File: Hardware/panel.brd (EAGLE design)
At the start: 79 x 43 mm, 86 parts, among them Q1 BC817-40LT1SMD, Q10 BC807-16LT1SMD, Q11 BC807-16LT1SMD, Q12 BC807-16LT1SMD, Q13 BC817-40LT1SMD, Q14 BC817-40LT1SMD, Q15 BC817-40LT1SMD, Q16 BC817-40LT1SMD, Q17 BC817-40LT1SMD, Q18 BC817-40LT1SMD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

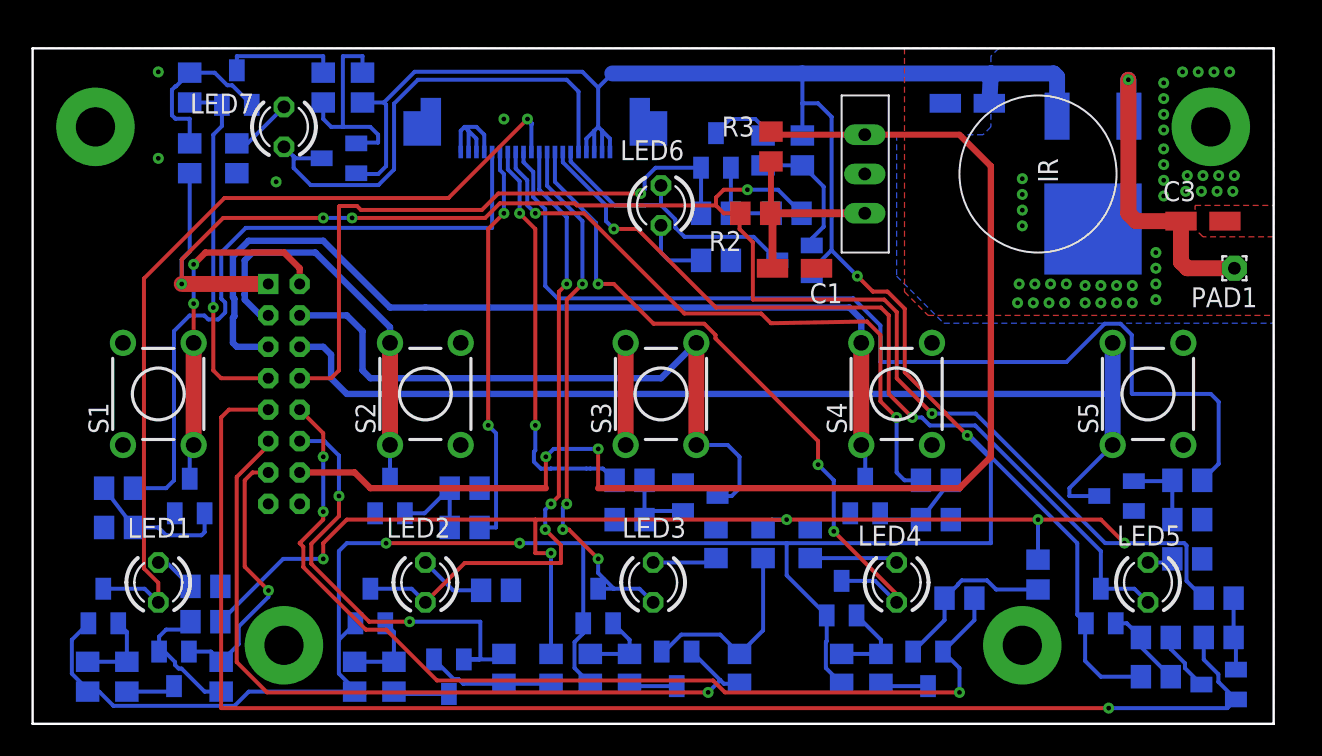
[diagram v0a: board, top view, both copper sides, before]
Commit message: по результатам эксперимента с кнопками и индикаторами все нормально. оявилась идея добавить защитные резисторы на индикаторные выходы,чтобы не сгорал транзистор в случае кз на землю
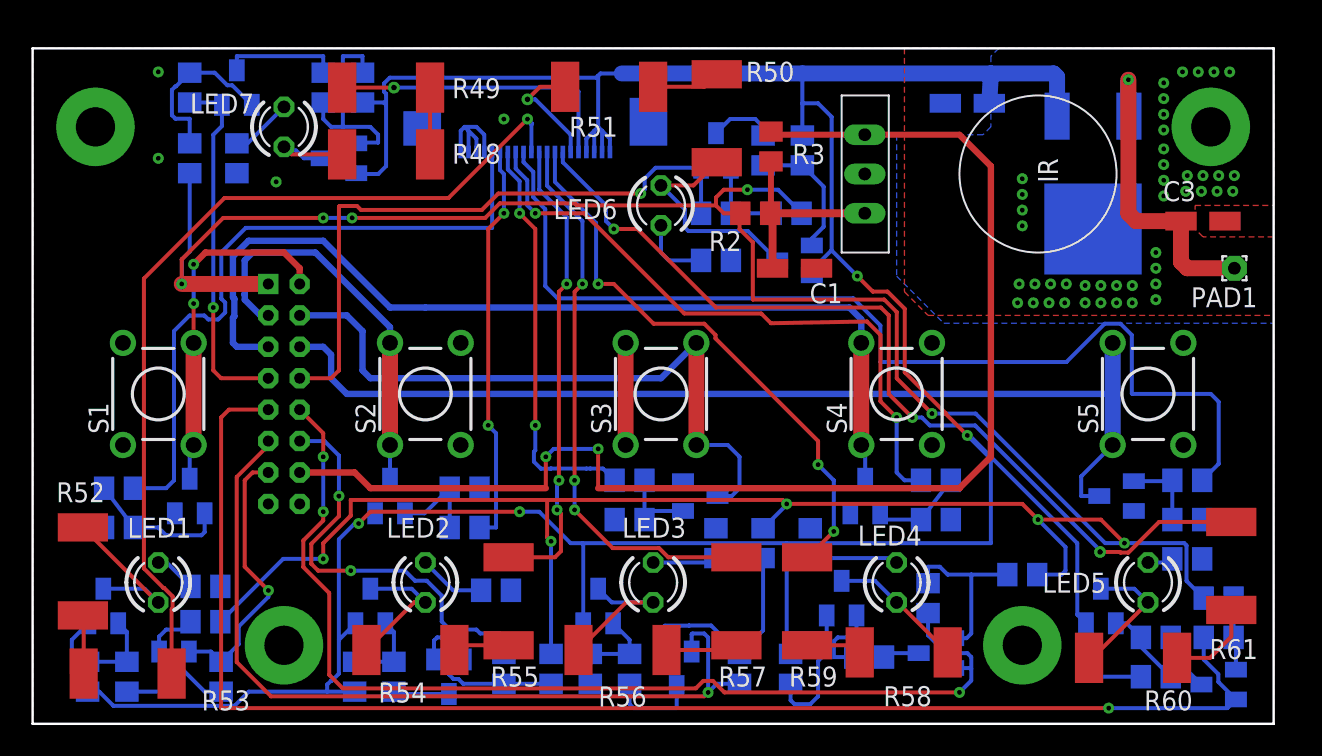
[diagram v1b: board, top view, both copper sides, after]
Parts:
- added R48, R49, R50, R51, R52, R53, R54, R55, R56, R57, R58, R59, R60, R61: 150, rcl:R2512
- moved R30 3.25 mm to (47.2, 2.50), turned to 90 degrees
- moved R40 2.00 mm to (56.0, 7.00), turned to 270 degrees
- moved Q16 1.12 mm to (56.5, 3.50), turned to 270 degrees
- moved R28 1.06 mm to (52.2, 3.25), turned to 180 degrees
- moved R41 1.00 mm to (62.0, 8.50), turned to 0 degrees
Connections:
- new net N$3: LED7.A, Q6.3, R48.1
- new net N$36: R48.2, R49.1
- new net N$37: LED6.A, Q7.3, R50.1
- new net N$38: R50.2, R51.1
- new net N$39: LED1.A, Q8.3, R52.1
- new net N$40: R52.2, R53.1
- new net N$41: LED2.A, Q9.3, R54.1
- new net N$42: R54.2, R55.1
- new net N$43: LED3.A, Q10.3, R56.1
- new net N$44: R56.2, R57.1
- new net N$45: LED4.A, Q11.3, R58.1
- new net N$46: R58.2, R59.1
- new net N$47: LED5.A, Q12.3, R60.1
- new net N$48: R60.2, R61.1
- net ADJLED_SIG: now also R55.2; no longer LED2.A, Q9.3
- net DOWNLED_SIG: now also R57.2; no longer LED3.A, Q10.3
- net LVLLED_SIG: now also R49.2; no longer LED7.A, Q6.3
- net PWRLED_SIG: now also R53.2; no longer LED1.A, Q8.3
- net UPLED_SIG: now also R51.2; no longer LED6.A, Q7.3
- net XLED_SIG: now also R59.2; no longer LED4.A, Q11.3
- net YLED_SIG: now also R61.2; no longer LED5.A, Q12.3
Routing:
- net N$37: track 0.00 -> 14.2 mm
- net LVLLED_SIG: track 31.4 -> 19.0 mm, vias 0 -> 1
- net ADJLED_SIG: track 41.4 -> 30.0 mm
- net N$39: track 0.00 -> 10.6 mm
- net UPLED_SIG: track 17.9 -> 7.51 mm, vias 0 -> 1
- net N$43: track 0.00 -> 9.87 mm
- net N$41: track 0.00 -> 8.87 mm
- net N$45: track 0.00 -> 8.63 mm
- net N$47: track 0.00 -> 8.57 mm
- net XLED_SIG: track 44.2 -> 36.4 mm
- net N$3: track 0.00 -> 6.60 mm
- net N$20: track 5.59 -> 11.5 mm
- net +5V: track 179.9 -> 185.7 mm
- net N$48: track 0.00 -> 5.71 mm
- net XLED: track 63.7 -> 68.3 mm
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
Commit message: подготовил файлы для заказа в электроконнекте,а так же сделал пдф со списком компонентов
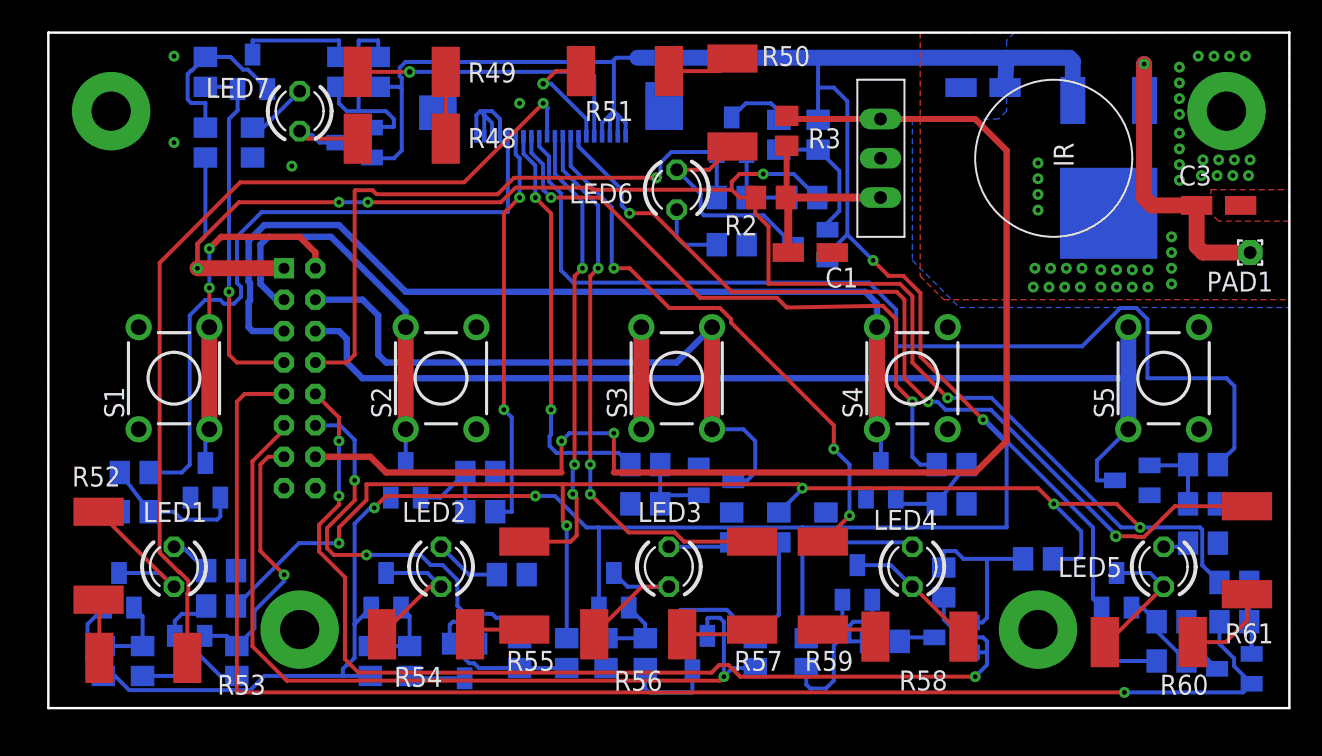
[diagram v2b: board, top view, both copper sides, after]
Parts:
- moved C1 1.41 mm to (48.5, 29.0)
- moved C2 1.41 mm to (59.5, 39.5)
- moved C3 1.41 mm to (74.5, 32.0)
- moved LED1 1.41 mm to (8.00, 9.00)
- moved LED2 1.41 mm to (25.0, 9.00)
- moved LED3 1.41 mm to (39.5, 9.00)
- moved LED4 1.41 mm to (55.0, 9.00)
- moved LED5 1.41 mm to (71.0, 9.00)
- moved LED6 1.41 mm to (40.0, 33.0)
- moved LED7 1.41 mm to (16.0, 38.0)
- moved PAD1 1.41 mm to (76.5, 29.0)
- moved Q1 1.41 mm to (10.0, 14.5)
- moved Q10 1.41 mm to (36.0, 7.50)
- moved Q11 1.41 mm to (51.5, 8.00)
- moved Q12 1.41 mm to (68.0, 7.50)
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
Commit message: по требованию с производства увеличил зазорполигона до 0,2мм на обеих платах. заказ переделал. заказе указал покрытие ПОС 63 вместо имерсионного олова
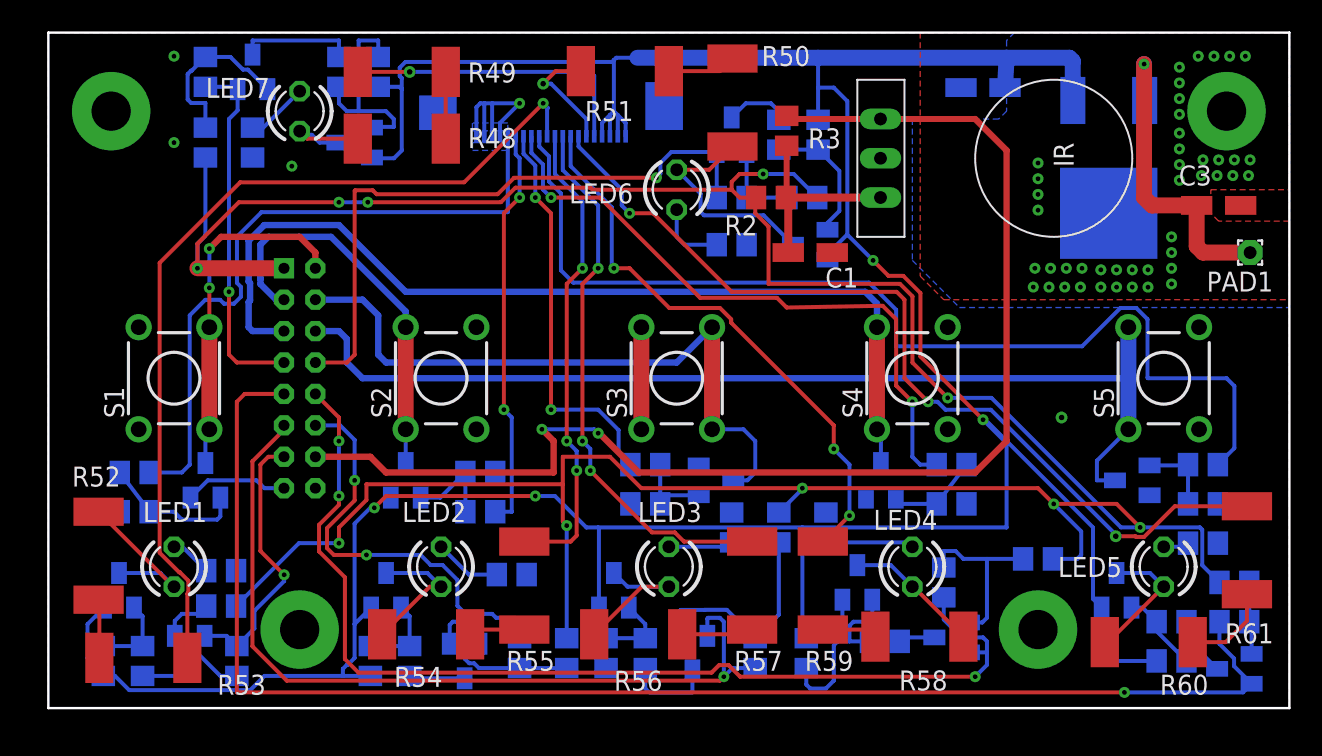
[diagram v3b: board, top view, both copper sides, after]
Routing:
- net GND: track 14.0 -> 24.6 mm, vias 52 -> 53
- net +5V: track 185.7 -> 188.1 mm
- net LASER_SIG: track 26.1 -> 25.5 mm
- added copper zone on layer 16, net GND1

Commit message: добавил RC-цепочку для устранения дребезга
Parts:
- added C4: 1uF, rcl:C0805
- added R62: 4.7k, rcl:R0805
- added R63: 200k, rcl:R0805
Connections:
- new net N$49: Q1.C, R62.1, R63.2, S1.2, S1.4
- net +5V: now also R62.2
- net GND: now also C4.2
- net PWR_SW: now also C4.1, R63.1; no longer Q1.C, S1.2, S1.4
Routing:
- net N$49: track 0.00 -> 23.7 mm
- net PWR_SW: track 22.2 -> 17.6 mm, vias 2 -> 1
- net PWRLED_SIG: track 56.8 -> 60.8 mm
- net +5V: track 188.1 -> 192.0 mm
- net +24V: track 226.1 -> 229.7 mm
- net UPLED_SIG: track 7.51 -> 8.41 mm
- net LVLLED_SIG: track 19.0 -> 19.9 mm

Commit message: экспеиментально подобрал параметры цепочки кнопки питания, чтобы она срабатывала без проблем
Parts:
- R63: value 200k -> 1k
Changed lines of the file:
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@@
 <attribute name="VALUE" x="9.385" y="30.46" size="1.27" layer="28" rot="MR0"/>
 </element>
-<element name="R63" library="rcl" library_urn="urn:adsk.eagle:library:334" package="R0805" package3d_urn="urn:adsk.eagle:package:23553/2" value="200k" x="6" y="27.25" smashed="yes" rot="MR180">
+<element name="R63" library="rcl" library_urn="urn:adsk.eagle:library:334" package="R0805" package3d_urn="urn:adsk.eagle:package:23553/2" value="1k" x="6" y="27.25" smashed="yes" rot="MR180">
 <attribute name="NAME" x="5.365" y="25.98" size="1.27" layer="26" rot="MR180"/>
 <attribute name="POPULARITY" value="86" x="6" y="27.25" size="1.778" layer="28" rot="MR180" display="off"/>
